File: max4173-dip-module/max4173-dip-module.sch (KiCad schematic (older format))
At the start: 5 parts, among them K1 CONN_3, K2 CONN_3, U1 MAX4173_SO8

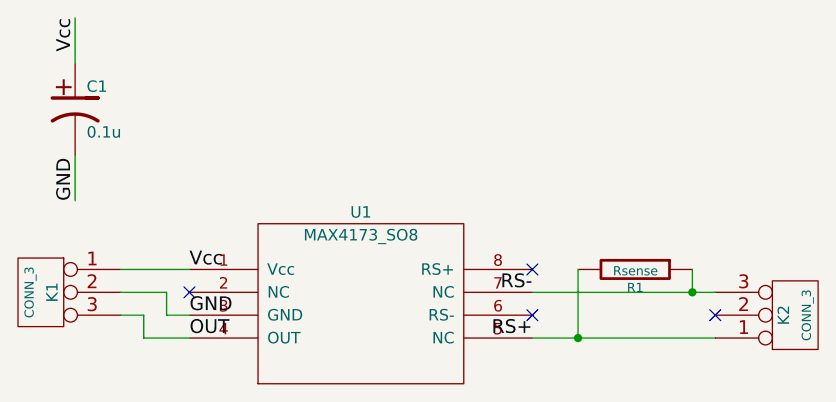
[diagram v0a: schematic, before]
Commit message: fixed pin numbering error on MAX4173 board
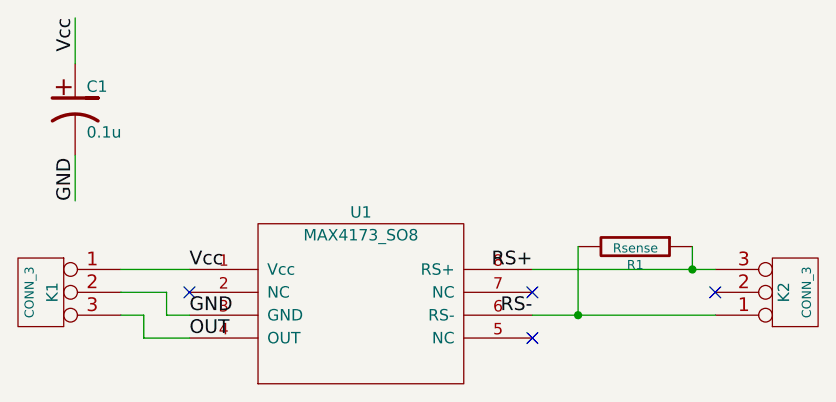
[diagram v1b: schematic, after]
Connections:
- net RS+: now also K2.3 (P3), R1.1, U1.8 (RS+); no longer K2.1 (P1), R1.2, U1.5 (NC)
- net RS-: now also K2.1 (P1), R1.2, U1.6 (RS-); no longer K2.3 (P3), R1.1, U1.7 (NC)
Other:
- moved on the sheet: K2, R1
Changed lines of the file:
@@
 Sheet 1 1
 Title ""
-Date "2 aug 2014"
+Date "15 aug 2014"
 Rev ""
 Comp ""
@@
 L CONN_3 K2
 U 1 1 53DC2825
-P 7650 3200
-F 0 "K2" V 7600 3200 50  0000 C CNN
-F 1 "CONN_3" V 7700 3200 40  0000 C CNN
-F 2 "~" H 7650 3200 60  0000 C CNN
-F 3 "~" H 7650 3200 60  0000 C CNN
-	1    7650 3200
+P 7650 3100
+F 0 "K2" V 7600 3100 50  0000 C CNN
+F 1 "CONN_3" V 7700 3100 40  0000 C CNN
+F 2 "~" H 7650 3100 60  0000 C CNN
+F 3 "~" H 7650 3100 60  0000 C CNN
+	1    7650 3100
 	1    0    0    1
 $EndComp
@@
 L R R1
 U 1 1 53DC2843
-P 6950 3000
-F 0 "R1" V 7030 3000 40  0000 C CNN
-F 1 "Rsense" V 6957 3001 40  0000 C CNN
-F 2 "~" V 6880 3000 30  0000 C CNN
-F 3 "~" H 6950 3000 30  0000 C CNN
-	1    6950 3000
+P 6950 2900
+F 0 "R1" V 7030 2900 40  0000 C CNN
+F 1 "Rsense" V 6957 2901 40  0000 C CNN
+F 2 "~" V 6880 2900 30  0000 C CNN
+F 3 "~" H 6950 2900 30  0000 C CNN
+	1    6950 2900
 	0    1    1    0
 $EndComp
@@
 	1    0    0    -1
 $EndComp
-Text Label 6500 3100 2    60   ~ 0
+Text Label 6500 3200 2    60   ~ 0
 RS-
-Text Label 6500 3300 2    60   ~ 0
+Text Label 6500 3000 2    60   ~ 0
 RS+
 Text Label 5000 3300 0    60   ~ 0
@@
 Wire Wire Line
 	4700 3000 5000 3000
-NoConn ~ 6500 3200
-NoConn ~ 6500 3000
+NoConn ~ 6500 3300
+NoConn ~ 6500 3100
 NoConn ~ 5000 3100
 Wire Wire Line
@@
 Wire Wire Line
 	4800 3300 5000 3300
-NoConn ~ 7300 3200
+NoConn ~ 7300 3100
 Wire Wire Line
 	4500 2100 4500 1900
@@
 	4500 2700 4500 2500
 Wire Wire Line
-	6500 3300 7300 3300
+	6500 3200 7300 3200
 Wire Wire Line
-	6500 3100 7300 3100
+	6500 3000 7300 3000
 Wire Wire Line
-	7200 3100 7200 3000
-Connection ~ 7200 3100
+	7200 3000 7200 2900
+Connection ~ 7200 3000
 Wire Wire Line
-	6700 3000 6700 3300
-Connection ~ 6700 3300
+	6700 2900 6700 3200
+Connection ~ 6700 3200
 $EndSCHEMATC
